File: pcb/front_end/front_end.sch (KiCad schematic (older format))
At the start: 44 parts

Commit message: Preliminary layout
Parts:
- FL2: renamed from FL?; value LPF_35GHz -> LPF 35GHz
- FL3: renamed from FL?; value LPF_35GHz -> Tuning LPF 35GHz
- FL4: renamed from FL?; value LPF_48GHz -> Infineon LPF 48GHz
- FL5: renamed from FL?; value LPF_Radial_Stub_30GHz -> LPF Radial Stub 30GHz
- J1, J10, J11, J12, J13, J14, J15, J16, J17, J18, J19, J2, J20, J21, J22, J23, J24, J25, J26, J27, J28, J29, J3, J30, J31, J4, J5, J6, J9: renamed from J?; footprint (none) -> bloop:292-06A-5; MPN (none) -> 292-06A-5
- J7, J8: renamed from J?; footprint (none) -> bloop:0734153320; MPN (none) -> 0734153320
- gave numbers to parts that had none: 9

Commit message: Add 100 ohm resistors to wilkinson dividers
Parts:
- added R? (x3): 100, symbol Device:R_US
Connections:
- wire segments 82 -> 88
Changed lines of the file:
@@
 $EndComp
 Wire Wire Line
-	8300 4250 7650 4250
-Wire Wire Line
-	8300 4550 8300 4250
-Wire Wire Line
-	8300 5150 7650 5150
-Wire Wire Line
-	8300 4850 8300 5150
+	8000 4250 7650 4250
+Wire Wire Line
+	8000 4550 8000 4250
+Wire Wire Line
+	8000 5150 7650 5150
+Wire Wire Line
+	8000 4850 8000 5150
 Wire Wire Line
 	7450 5350 7450 5400
@@
 	1    0    0    -1
 $EndComp
-Wire Wire Line
-	8550 4850 8300 4850
-Wire Wire Line
-	8550 4550 8300 4550
 Wire Wire Line
 	9450 4700 10100 4700
@@
 $EndComp
 Wire Wire Line
-	8300 6250 7650 6250
-Wire Wire Line
-	8300 6550 8300 6250
-Wire Wire Line
-	8300 7150 7650 7150
-Wire Wire Line
-	8300 6850 8300 7150
-Wire Wire Line
 	7450 7350 7450 7400
 Wire Wire Line
@@
 	1    0    0    -1
 $EndComp
-Wire Wire Line
-	8550 6850 8300 6850
-Wire Wire Line
-	8550 6550 8300 6550
 Wire Wire Line
 	9450 6700 10100 6700
@@
 $EndComp
 Wire Wire Line
-	8300 8250 7650 8250
-Wire Wire Line
-	8300 8550 8300 8250
-Wire Wire Line
-	8300 9150 7650 9150
-Wire Wire Line
-	8300 8850 8300 9150
-Wire Wire Line
 	7450 9350 7450 9400
 Wire Wire Line
@@
 	1    0    0    -1
 $EndComp
-Wire Wire Line
-	8550 8850 8300 8850
-Wire Wire Line
-	8550 8550 8300 8550
 Wire Wire Line
 	9450 8700 10100 8700
@@
 	-1   0    0    -1
 $EndComp
+$Comp
+L Device:R_US R?
+U 1 1 5D4F9AA7
+P 8250 4700
+F 0 "R?" H 8318 4746 50  0000 L CNN
+F 1 "100" H 8318 4655 50  0000 L CNN
+F 2 "" V 8290 4690 50  0001 C CNN
+F 3 "~" H 8250 4700 50  0001 C CNN
+	1    8250 4700
+	1    0    0    -1
+$EndComp
+Wire Wire Line
+	8000 4850 8250 4850
+Wire Wire Line
+	8000 4550 8250 4550
+Connection ~ 8250 4550
+Wire Wire Line
+	8250 4550 8550 4550
+Connection ~ 8250 4850
+Wire Wire Line
+	8250 4850 8550 4850
+Wire Wire Line
+	8000 6250 7650 6250
+Wire Wire Line
+	8000 6550 8000 6250
+Wire Wire Line
+	8000 7150 7650 7150
+Wire Wire Line
+	8000 6850 8000 7150
+$Comp
+L Device:R_US R?
+U 1 1 5D511FA6
+P 8250 6700
+F 0 "R?" H 8318 6746 50  0000 L CNN
+F 1 "100" H 8318 6655 50  0000 L CNN
+F 2 "" V 8290 6690 50  0001 C CNN
+F 3 "~" H 8250 6700 50  0001 C CNN
+	1    8250 6700
+	1    0    0    -1
+$EndComp
+Wire Wire Line
+	8000 6850 8250 6850
+Wire Wire Line
+	8000 6550 8250 6550
+Connection ~ 8250 6550
+Wire Wire Line
+	8250 6550 8550 6550
+Connection ~ 8250 6850
+Wire Wire Line
+	8250 6850 8550 6850
+Wire Wire Line
+	8000 8250 7650 8250
+Wire Wire Line
+	8000 8550 8000 8250
+Wire Wire Line
+	8000 9150 7650 9150
+Wire Wire Line
+	8000 8850 8000 9150
+$Comp
+L Device:R_US R?
+U 1 1 5D514628
+P 8250 8700
+F 0 "R?" H 8318 8746 50  0000 L CNN
+F 1 "100" H 8318 8655 50  0000 L CNN
+F 2 "" V 8290 8690 50  0001 C CNN
+F 3 "~" H 8250 8700 50  0001 C CNN
+	1    8250 8700
+	1    0    0    -1
+$EndComp
+Wire Wire Line
+	8000 8850 8250 8850
+Wire Wire Line
+	8000 8550 8250 8550
+Connection ~ 8250 8550
+Wire Wire Line
+	8250 8550 8550 8550
+Connection ~ 8250 8850
+Wire Wire Line
+	8250 8850 8550 8850
 $EndSCHEMATC

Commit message: Updates to front end layout
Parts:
- removed R? (x3): 100, symbol Device:R_US
- added TM1: OPEN_Zo, bloop:OPEN_21mil, symbol bloop:OPEN_Zo
- C1, C2: footprint (none) -> bloop:DC_Block
- WLK1, WLK2, WLK3, WLK4: footprint (none) -> bloop:Wilkinson_V1
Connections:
- wire segments 88 -> 82
- no-connect marks 1 -> 0
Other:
- note added: "LINE 1 = 1.253 in\n"
- note added: "OPEN = 0.5897 in"
- note added: "THRU = 1.1794 in\n"
- note removed: "LINE 1 = ?"
- note removed: "OPEN = ?"
- note removed: "THRU = ?"
- moved on the sheet: J4, J6, J7
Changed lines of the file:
@@
 EESchema Schematic File Version 4
 LIBS:front_end-cache
-EELAYER 30 0
+EELAYER 29 0
 EELAYER END
 $Descr B 17000 11000
@@
 Wire Wire Line
 	7700 2000 7450 2000
-Wire Wire Line
-	11050 2050 11050 2150
 $Comp
 L power:GND #PWR0101
@@
 $EndComp
 Wire Wire Line
-	9500 1850 9850 1850
-Wire Wire Line
 	10500 1850 10500 2000
 Wire Wire Line
@@
 Wire Wire Line
 	10500 1850 10850 1850
-Connection ~ 10500 1850
-Wire Wire Line
-	10150 1850 10500 1850
 Wire Wire Line
 	14150 1700 14150 1750
@@
 	13100 1500 12550 1500
 Wire Wire Line
-	4600 2650 4600 2700
+	5000 2650 5000 2700
 $Comp
 L power:GND #PWR0107
 U 1 1 5D4E6E63
-P 4600 2700
-F 0 "#PWR0107" H 4600 2450 50  0001 C CNN
-F 1 "GND" H 4605 2527 50  0000 C CNN
-F 2 "" H 4600 2700 50  0001 C CNN
-F 3 "" H 4600 2700 50  0001 C CNN
-	1    4600 2700
+P 5000 2700
+F 0 "#PWR0107" H 5000 2450 50  0001 C CNN
+F 1 "GND" H 5005 2527 50  0000 C CNN
+F 2 "" H 5000 2700 50  0001 C CNN
+F 3 "" H 5000 2700 50  0001 C CNN
+	1    5000 2700
 	1    0    0    -1
 $EndComp
@@
 	3200 2650 3200 2700
 Wire Wire Line
-	3400 2450 4400 2450
-Text Notes 3800 2400 0    50   ~ 0
-THRU = ?
+	3400 2450 4800 2450
+Text Notes 3750 2400 0    50   ~ 0
+THRU = 1.1794 in\n
 $Comp
 L bloop:LPF_35GHz FL1
@@
 F 0 "WLK1" H 8150 2265 50  0000 C CNN
 F 1 "WILK_24_GHZ" H 8150 2174 50  0000 C CNN
-F 2 "" H 8150 2200 50  0001 C CNN
+F 2 "bloop:Wilkinson_V1" H 8150 2200 50  0001 C CNN
 F 3 "" H 8150 2200 50  0001 C CNN
 	1    8150 1850
@@
 F 0 "C1" V 9748 1850 50  0000 C CNN
 F 1 "DC BLK" V 9839 1850 50  0000 C CNN
-F 2 "" H 10038 1700 50  0001 C CNN
+F 2 "bloop:DC_Block" H 10038 1700 50  0001 C CNN
 F 3 "~" H 10000 1850 50  0001 C CNN
 	1    10000 1850
@@
 F 0 "C2" V 12998 1500 50  0000 C CNN
 F 1 "DC BLK" V 13089 1500 50  0000 C CNN
-F 2 "" H 13288 1350 50  0001 C CNN
+F 2 "bloop:DC_Block" H 13288 1350 50  0001 C CNN
 F 3 "~" H 13250 1500 50  0001 C CNN
 	1    13250 1500
@@
 L Connector:Conn_Coaxial J6
 U 1 1 5D4E6E5C
-P 4600 2450
-F 0 "J6" H 4700 2550 50  0000 L CNN
-F 1 "SMA" H 4700 2450 50  0000 L CNN
-F 2 "bloop:292-06A-5" H 4600 2450 50  0001 C CNN
-F 3 "https://www.hasco-inc.com/content/Southwest/End%20Launch/Jack/SMA_jack_endlaunch_genoutline.pdf" H 4600 2450 50  0001 C CNN
-F 4 "292-06A-5" H 4600 2450 50  0001 C CNN "MPN"
-	1    4600 2450
+P 5000 2450
+F 0 "J6" H 5100 2550 50  0000 L CNN
+F 1 "SMA" H 5100 2450 50  0000 L CNN
+F 2 "bloop:292-06A-5" H 5000 2450 50  0001 C CNN
+F 3 "https://www.hasco-inc.com/content/Southwest/End%20Launch/Jack/SMA_jack_endlaunch_genoutline.pdf" H 5000 2450 50  0001 C CNN
+F 4 "292-06A-5" H 5000 2450 50  0001 C CNN "MPN"
+	1    5000 2450
 	1    0    0    -1
 $EndComp
@@
 Wire Wire Line
 	3400 1350 5250 1350
-Text Notes 3800 1300 0    50   ~ 0
-LINE 1 = ?
+Text Notes 3900 1300 0    50   ~ 0
+LINE 1 = 1.253 in\n
 $Comp
 L Connector:Conn_Coaxial J9
@@
 	3200 3650 3200 3700
 Wire Wire Line
-	3400 3450 3800 3450
-Text Notes 3800 3400 0    50   ~ 0
-OPEN = ?
+	3400 3450 4100 3450
+Text Notes 3400 3300 0    50   ~ 0
+OPEN = 0.5897 in
 $Comp
 L Connector:Conn_Coaxial J3
@@
 	-1   0    0    -1
 $EndComp
-NoConn ~ 3800 3450
 Wire Notes Line
 	2600 750  2600 4150
@@
 F 0 "WLK2" H 9000 5115 50  0000 C CNN
 F 1 "WILK_24_GHZ" H 9000 5024 50  0000 C CNN
-F 2 "" H 9000 5050 50  0001 C CNN
+F 2 "bloop:Wilkinson_V1" H 9000 5050 50  0001 C CNN
 F 3 "" H 9000 5050 50  0001 C CNN
 	1    9000 4700
@@
 Wire Wire Line
 	10300 4900 10300 5000
-Text Notes 4050 5100 0    59   ~ 12
+Text Notes 4750 4950 0    59   ~ 12
 SMP Bullet
 Wire Notes Line style solid
-	3850 5200 3950 5200
-Wire Wire Line
-	3650 5250 4950 5250
+	4550 5050 4650 5050
 Wire Notes Line style solid
-	3850 5300 3850 5200
+	4550 5150 4550 5050
 Wire Notes Line style solid
-	3950 5300 3850 5300
+	4650 5150 4550 5150
 Wire Notes Line style solid
-	4650 5350 3950 5350
+	5350 5200 4650 5200
 Wire Notes Line style solid
-	4750 5300 4650 5300
+	5450 5150 5350 5150
 Wire Notes Line style solid
-	4750 5200 4750 5300
+	5450 5050 5450 5150
 Wire Notes Line style solid
-	4650 5200 4750 5200
+	5350 5050 5450 5050
 Wire Notes Line style solid
-	3950 5150 4650 5150
+	4650 5000 5350 5000
 $Comp
 L Connector:Conn_Coaxial J7
 U 1 1 5D534F40
-P 5150 5250
-F 0 "J7" H 5250 5350 50  0000 L CNN
-F 1 "SMP" H 5250 5250 50  0000 L CNN
-F 2 "bloop:0734153320" H 5150 5250 50  0001 C CNN
-F 3 "https://www.molex.com/webdocs/datasheets/pdf/en-us/0734153320_RF_COAX_CONNECTORS.pdf" H 5150 5250 50  0001 C CNN
-F 4 "0734153320" H 5150 5250 50  0001 C CNN "MPN"
-	1    5150 5250
+P 4250 5100
+F 0 "J7" H 4350 5200 50  0000 L CNN
+F 1 "SMP" H 4350 5100 50  0000 L CNN
+F 2 "bloop:0734153320" H 4250 5100 50  0001 C CNN
+F 3 "https://www.molex.com/webdocs/datasheets/pdf/en-us/0734153320_RF_COAX_CONNECTORS.pdf" H 4250 5100 50  0001 C CNN
+F 4 "0734153320" H 4250 5100 50  0001 C CNN "MPN"
+	1    4250 5100
 	1    0    0    -1
 $EndComp
@@
 L power:GND #PWR0117
 U 1 1 5D534F3A
-P 5150 5550
-F 0 "#PWR0117" H 5150 5300 50  0001 C CNN
-F 1 "GND" H 5155 5377 50  0000 C CNN
-F 2 "" H 5150 5550 50  0001 C CNN
-F 3 "" H 5150 5550 50  0001 C CNN
-	1    5150 5550
-	1    0    0    -1
-$EndComp
-Wire Wire Line
-	5150 5450 5150 5550
+P 4250 5400
+F 0 "#PWR0117" H 4250 5150 50  0001 C CNN
+F 1 "GND" H 4255 5227 50  0000 C CNN
+F 2 "" H 4250 5400 50  0001 C CNN
+F 3 "" H 4250 5400 50  0001 C CNN
+	1    4250 5400
+	1    0    0    -1
+$EndComp
+Wire Wire Line
+	4250 5300 4250 5400
 $Comp
 L power:GND #PWR0118
 U 1 1 5D534F31
-P 3450 5500
-F 0 "#PWR0118" H 3450 5250 50  0001 C CNN
-F 1 "GND" H 3455 5327 50  0000 C CNN
-F 2 "" H 3450 5500 50  0001 C CNN
-F 3 "" H 3450 5500 50  0001 C CNN
-	1    3450 5500
-	1    0    0    -1
-$EndComp
-Wire Wire Line
-	3450 5450 3450 5500
+P 3450 5350
+F 0 "#PWR0118" H 3450 5100 50  0001 C CNN
+F 1 "GND" H 3455 5177 50  0000 C CNN
+F 2 "" H 3450 5350 50  0001 C CNN
+F 3 "" H 3450 5350 50  0001 C CNN
+	1    3450 5350
+	1    0    0    -1
+$EndComp
+Wire Wire Line
+	3450 5300 3450 5350
 $Comp
 L Connector:Conn_Coaxial J4
 U 1 1 5D534F2A
-P 3450 5250
-F 0 "J4" H 3650 5350 50  0000 C CNN
-F 1 "SMA" H 3650 5250 50  0000 C CNN
-F 2 "bloop:292-06A-5" H 3450 5250 50  0001 C CNN
-F 3 "https://www.hasco-inc.com/content/Southwest/End%20Launch/Jack/SMA_jack_endlaunch_genoutline.pdf" H 3450 5250 50  0001 C CNN
-F 4 "292-06A-5" H 3450 5250 50  0001 C CNN "MPN"
-	1    3450 5250
+P 3450 5100
+F 0 "J4" H 3650 5200 50  0000 C CNN
+F 1 "SMA" H 3650 5100 50  0000 C CNN
+F 2 "bloop:292-06A-5" H 3450 5100 50  0001 C CNN
+F 3 "https://www.hasco-inc.com/content/Southwest/End%20Launch/Jack/SMA_jack_endlaunch_genoutline.pdf" H 3450 5100 50  0001 C CNN
+F 4 "292-06A-5" H 3450 5100 50  0001 C CNN "MPN"
+	1    3450 5100
 	-1   0    0    -1
 $EndComp
@@
 F 0 "WLK3" H 9000 7115 50  0000 C CNN
 F 1 "WILK_24_GHZ" H 9000 7024 50  0000 C CNN
-F 2 "" H 9000 7050 50  0001 C CNN
+F 2 "bloop:Wilkinson_V1" H 9000 7050 50  0001 C CNN
 F 3 "" H 9000 7050 50  0001 C CNN
 	1    9000 6700
@@
 F 0 "WLK4" H 9000 9115 50  0000 C CNN
 F 1 "WILK_24_GHZ" H 9000 9024 50  0000 C CNN
-F 2 "" H 9000 9050 50  0001 C CNN
+F 2 "bloop:Wilkinson_V1" H 9000 9050 50  0001 C CNN
 F 3 "" H 9000 9050 50  0001 C CNN
 	1    9000 8700
@@
 Wilkinson Power Dividers
 Wire Notes Line style solid
-	3950 5150 3950 5350
+	4650 5000 4650 5200
 Wire Notes Line style solid
-	4650 5150 4650 5350
+	5350 5000 5350 5200
 Wire Notes Line
 	2600 4250 6050 4250
@@
 	-1   0    0    -1
 $EndComp
-$Comp
-L Device:R_US R?
-U 1 1 5D4F9AA7
-P 8250 4700
-F 0 "R?" H 8318 4746 50  0000 L CNN
-F 1 "100" H 8318 4655 50  0000 L CNN
-F 2 "" V 8290 4690 50  0001 C CNN
-F 3 "~" H 8250 4700 50  0001 C CNN
-	1    8250 4700
-	1    0    0    -1
-$EndComp
-Wire Wire Line
-	8000 4850 8250 4850
-Wire Wire Line
-	8000 4550 8250 4550
-Connection ~ 8250 4550
-Wire Wire Line
-	8250 4550 8550 4550
-Connection ~ 8250 4850
-Wire Wire Line
-	8250 4850 8550 4850
 Wire Wire Line
 	8000 6250 7650 6250
@@
 Wire Wire Line
 	8000 6850 8000 7150
-$Comp
-L Device:R_US R?
-U 1 1 5D511FA6
-P 8250 6700
-F 0 "R?" H 8318 6746 50  0000 L CNN
-F 1 "100" H 8318 6655 50  0000 L CNN
-F 2 "" V 8290 6690 50  0001 C CNN
-F 3 "~" H 8250 6700 50  0001 C CNN
-	1    8250 6700
-	1    0    0    -1
-$EndComp
-Wire Wire Line
-	8000 6850 8250 6850
-Wire Wire Line
-	8000 6550 8250 6550
-Connection ~ 8250 6550
-Wire Wire Line
-	8250 6550 8550 6550
-Connection ~ 8250 6850
-Wire Wire Line
-	8250 6850 8550 6850
 Wire Wire Line
 	8000 8250 7650 8250
@@
 Wire Wire Line
 	8000 8850 8000 9150
-$Comp
-L Device:R_US R?
-U 1 1 5D514628
-P 8250 8700
-F 0 "R?" H 8318 8746 50  0000 L CNN
-F 1 "100" H 8318 8655 50  0000 L CNN
-F 2 "" V 8290 8690 50  0001 C CNN
-F 3 "~" H 8250 8700 50  0001 C CNN
-	1    8250 8700
-	1    0    0    -1
-$EndComp
-Wire Wire Line
-	8000 8850 8250 8850
-Wire Wire Line
-	8000 8550 8250 8550
-Connection ~ 8250 8550
-Wire Wire Line
-	8250 8550 8550 8550
-Connection ~ 8250 8850
-Wire Wire Line
-	8250 8850 8550 8850
+Wire Wire Line
+	8000 4550 8550 4550
+Wire Wire Line
+	8000 4850 8550 4850
+Wire Wire Line
+	8000 6550 8550 6550
+Wire Wire Line
+	8000 6850 8550 6850
+Wire Wire Line
+	8000 8550 8550 8550
+Wire Wire Line
+	8000 8850 8550 8850
+$Comp
+L bloop:OPEN_Zo TM1
+U 1 1 5D556699
+P 4100 3450
+F 0 "TM1" H 4278 3514 50  0000 L CNN
+F 1 "OPEN_Zo" H 4278 3423 50  0000 L CNN
+F 2 "bloop:OPEN_21mil" H 4100 3600 50  0001 C CNN
+F 3 "" H 4100 3600 50  0001 C CNN
+	1    4100 3450
+	1    0    0    -1
+$EndComp
+Wire Wire Line
+	9850 1850 9500 1850
+Wire Wire Line
+	10150 1850 10500 1850
+Connection ~ 10500 1850
+Wire Wire Line
+	3650 5100 4050 5100
+Wire Wire Line
+	11050 2050 11050 2150
 $EndSCHEMATC

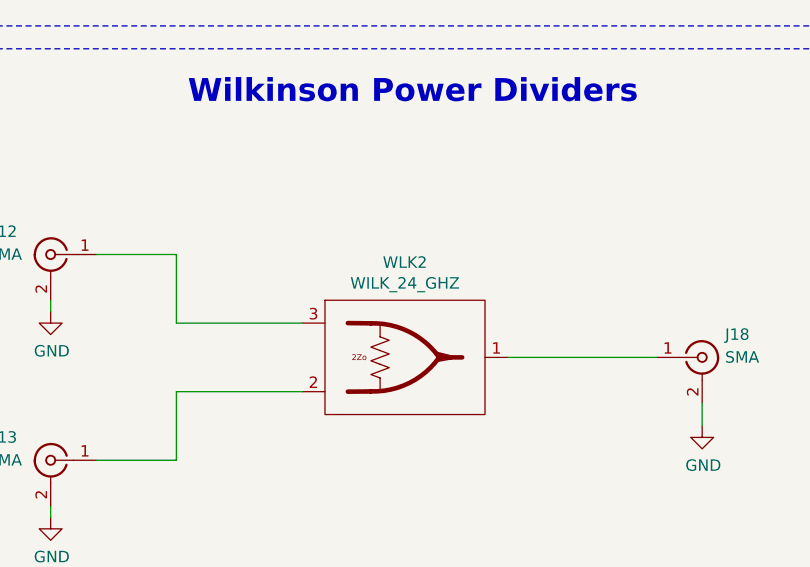
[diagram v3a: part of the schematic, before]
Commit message: Added Infineon Wilkinson
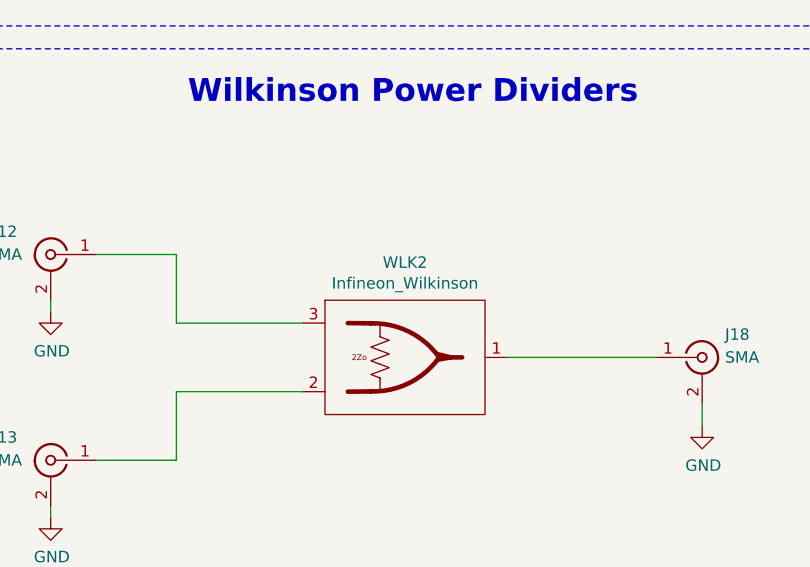
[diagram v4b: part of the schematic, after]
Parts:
- WLK2: value WILK_24_GHZ -> Infineon_Wilkinson; footprint bloop:Wilkinson_V1 -> bloop:Infineon_Wilkinson
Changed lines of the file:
@@
 P 9000 4700
 F 0 "WLK2" H 9000 5115 50  0000 C CNN
-F 1 "WILK_24_GHZ" H 9000 5024 50  0000 C CNN
-F 2 "bloop:Wilkinson_V1" H 9000 5050 50  0001 C CNN
+F 1 "Infineon_Wilkinson" H 9000 5024 50  0000 C CNN
+F 2 "bloop:Infineon_Wilkinson" H 9000 5050 50  0001 C CNN
 F 3 "" H 9000 5050 50  0001 C CNN
 	1    9000 4700

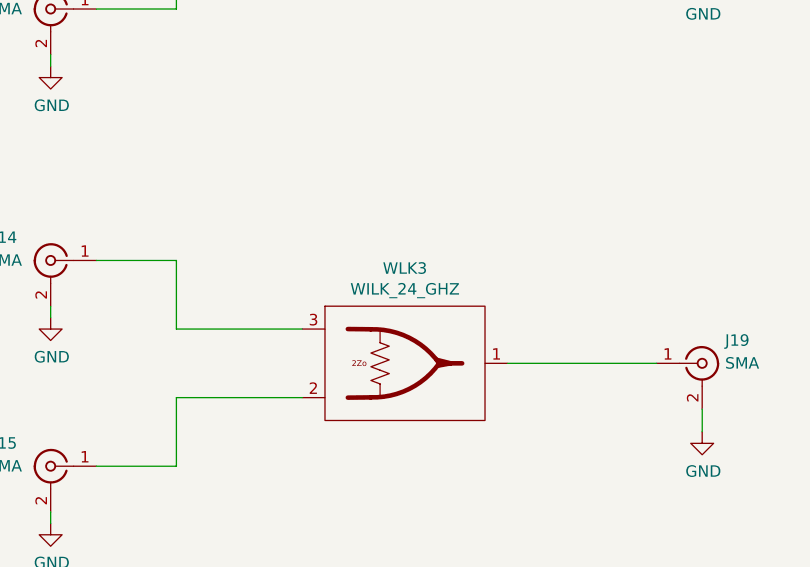
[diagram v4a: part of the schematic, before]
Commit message: Added Taper 8 24Ghz wilk/matched on PCB
Added Taper 8 24Ghz wilk/matched on PCB
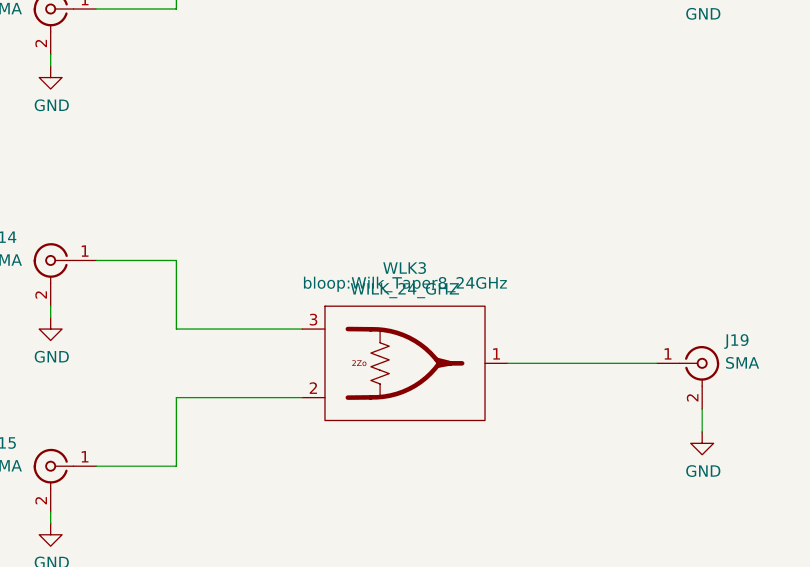
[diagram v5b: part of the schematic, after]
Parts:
- WLK3: footprint bloop:Wilkinson_V1 -> bloop:Wilk_Taper8_24GHz
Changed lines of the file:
@@
 F 0 "WLK3" H 9000 7115 50  0000 C CNN
 F 1 "WILK_24_GHZ" H 9000 7024 50  0000 C CNN
-F 2 "bloop:Wilkinson_V1" H 9000 7050 50  0001 C CNN
+F 2 "bloop:Wilk_Taper8_24GHz" H 9000 7050 50  0000 C CNN
 F 3 "" H 9000 7050 50  0001 C CNN
 	1    9000 6700
